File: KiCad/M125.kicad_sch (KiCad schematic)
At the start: 20 parts, among them J1 Conn_01x04, J2 Conn_01x04, J3 Shelly, Q1 PMF250XNEX, U1 ESP32-PICO-MINI-02, U2 LMR16006+FB

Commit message: New PCB
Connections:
- net B: now also U1.35 (IO21); no longer U1.27 (IO7)
- net DATA: now also U1.12 (IO32); no longer U1.21 (IO15)
- net NFCRX: now also U1.28 (IO8); no longer U1.20 (IO13)
- net NFCTX: now also U1.27 (IO7); no longer U1.18 (IO14)
- net SEND: now also U1.13 (IO33); no longer U1.28 (IO8)
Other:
- title: Generic ESP32-PICO-MINI module -> M-125 control
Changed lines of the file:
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@@
   (paper "A4")
   (title_block
-    (title "Generic ESP32-PICO-MINI module")
+    (title "M-125 control")
     (date "${DATE}")
     (rev "1")
@@
   (no_connect (at 50.8 66.04))
   (no_connect (at 50.8 71.12))
-  (no_connect (at 50.8 78.74))
-  (no_connect (at 81.28 68.58))
-  (no_connect (at 81.28 81.28))
-  (no_connect (at 81.28 83.82))
+  (no_connect (at 50.8 81.28))
+  (no_connect (at 91.44 76.2))
+  (no_connect (at 91.44 78.74))
+  (no_connect (at 91.44 81.28))
   (wire (pts (xy 220.98 38.1) (xy 231.775 38.1))
     (stroke (width 0) (type default) (color 0 0 0 0))
@@
     )
   )
-  (global_label "NFCRX" (shape input) (at 50.8 81.28 180) (fields_autoplaced)
-    (effects (font (size 1.27 1.27)) (justify right))
-    (property "Intersheet References" "${INTERSHEET_REFS}" (id 0) (at 42.3072 81.2006 0)
+  (global_label "NFCRX" (shape input) (at 50.8 76.2 180) (fields_autoplaced)
+    (effects (font (size 1.27 1.27)) (justify right))
+    (property "Intersheet References" "${INTERSHEET_REFS}" (id 0) (at 42.3072 76.1206 0)
       (effects (font (size 1.27 1.27)) (justify right) hide)
     )
@@
     )
   )
-  (global_label "SEND" (shape output) (at 50.8 76.2 180) (fields_autoplaced)
-    (effects (font (size 1.27 1.27)) (justify right))
-    (property "Intersheet References" "${INTERSHEET_REFS}" (id 0) (at 43.5168 76.1206 0)
-      (effects (font (size 1.27 1.27)) (justify right) hide)
+  (global_label "SEND" (shape output) (at 81.28 83.82 0) (fields_autoplaced)
+    (effects (font (size 1.27 1.27)) (justify left))
+    (property "Intersheet References" "${INTERSHEET_REFS}" (id 0) (at 88.5632 83.8994 0)
+      (effects (font (size 1.27 1.27)) (justify left) hide)
     )
   )
@@
     )
   )
-  (global_label "DATA" (shape input) (at 50.8 86.36 180) (fields_autoplaced)
-    (effects (font (size 1.27 1.27)) (justify right))
-    (property "Intersheet References" "${INTERSHEET_REFS}" (id 0) (at 44.061 86.2806 0)
-      (effects (font (size 1.27 1.27)) (justify right) hide)
+  (global_label "DATA" (shape input) (at 81.28 81.28 0) (fields_autoplaced)
+    (effects (font (size 1.27 1.27)) (justify left))
+    (property "Intersheet References" "${INTERSHEET_REFS}" (id 0) (at 88.019 81.3594 0)
+      (effects (font (size 1.27 1.27)) (justify left) hide)
     )
   )
@@
     )
   )
-  (global_label "NFCTX" (shape input) (at 50.8 83.82 180) (fields_autoplaced)
-    (effects (font (size 1.27 1.27)) (justify right))
-    (property "Intersheet References" "${INTERSHEET_REFS}" (id 0) (at 42.6096 83.7406 0)
+  (global_label "NFCTX" (shape input) (at 50.8 73.66 180) (fields_autoplaced)
+    (effects (font (size 1.27 1.27)) (justify right))
+    (property "Intersheet References" "${INTERSHEET_REFS}" (id 0) (at 42.6096 73.5806 0)
       (effects (font (size 1.27 1.27)) (justify right) hide)
     )
@@
     )
   )
-  (global_label "B" (shape input) (at 50.8 73.66 180) (fields_autoplaced)
-    (effects (font (size 1.27 1.27)) (justify right))
-    (property "Intersheet References" "${INTERSHEET_REFS}" (id 0) (at -52.07 -31.75 0)
-      (effects (font (size 1.27 1.27)) hide)
-    )
+  (global_label "B" (shape input) (at 81.28 68.58 0) (fields_autoplaced)
+    (effects (font (size 1.27 1.27)) (justify left))
+    (property "Intersheet References" "${INTERSHEET_REFS}" (id 0) (at 184.15 173.99 0)
+      (effects (font (size 1.27 1.27)) hide)
+    )

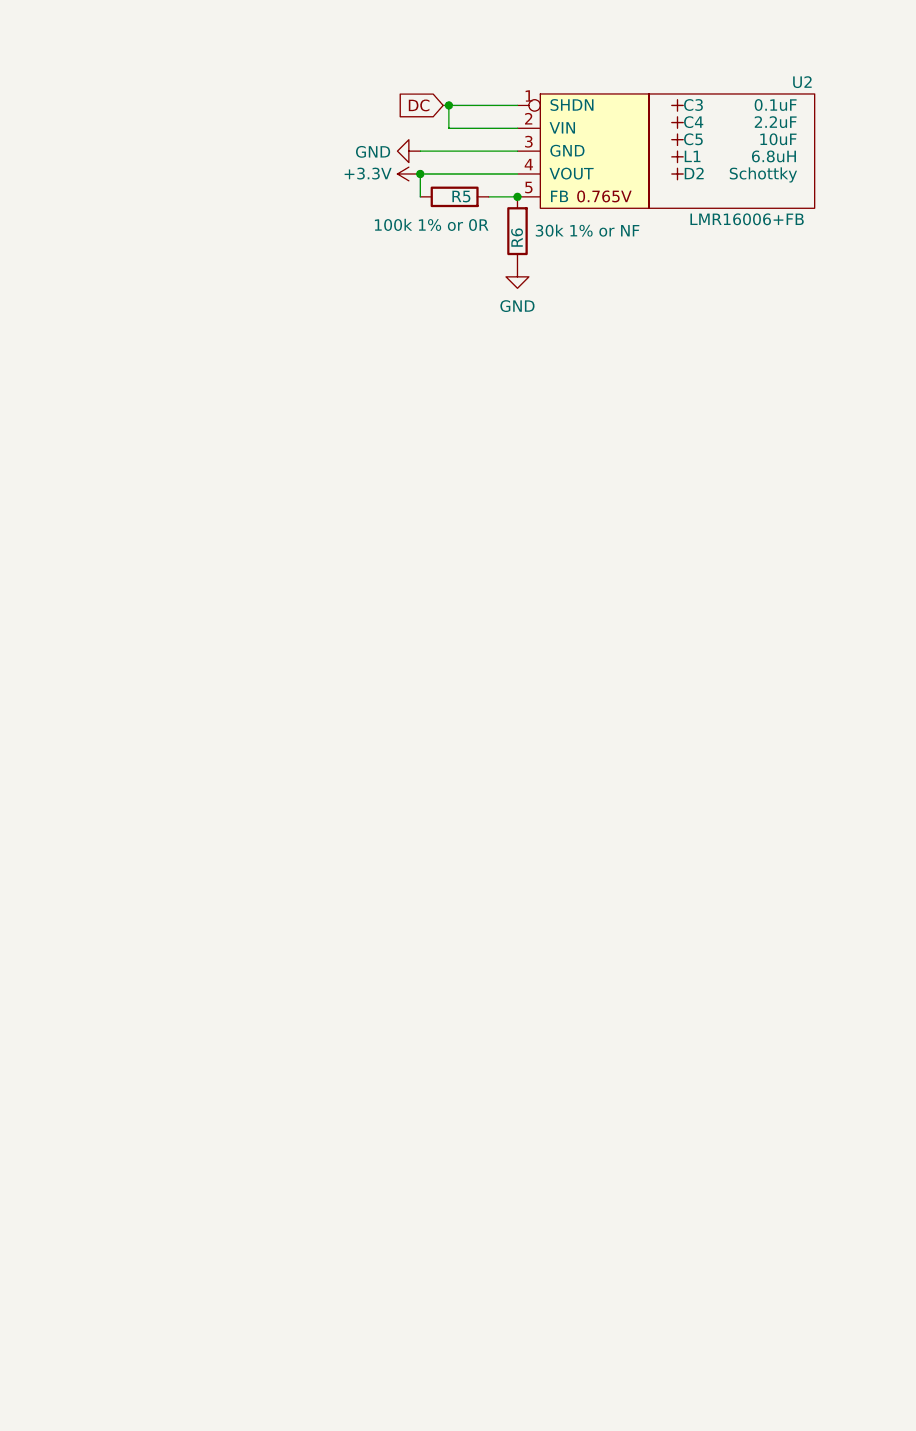
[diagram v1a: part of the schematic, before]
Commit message: Tidy PCB for placement of regulator parts
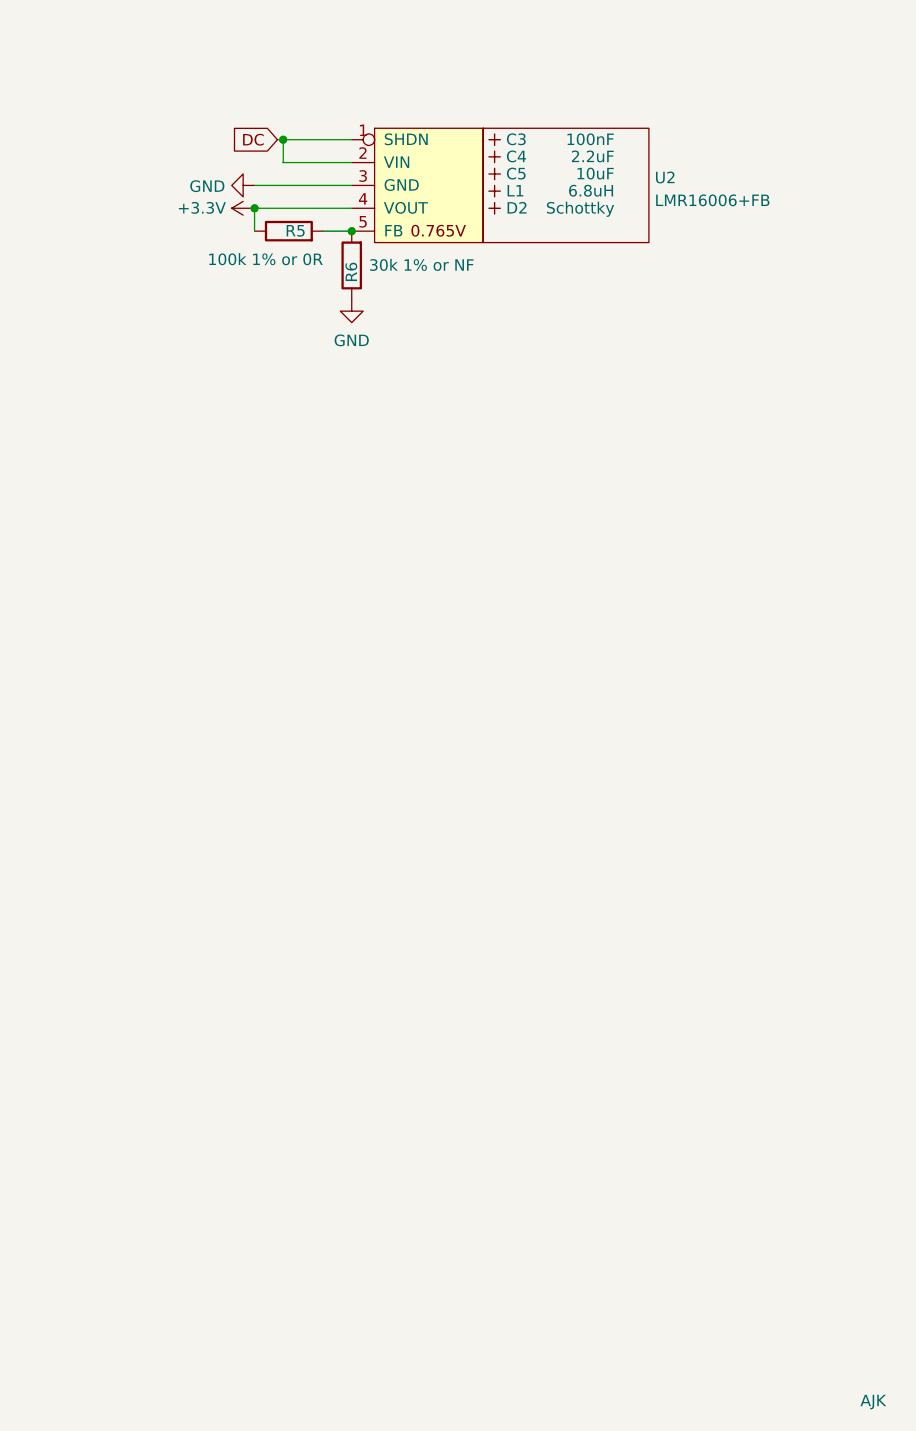
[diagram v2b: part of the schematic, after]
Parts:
- added Logo1: AJK, RevK:AJK, symbol RevK:AJK
- C3: value 0.1uF -> 100nF; footprint RevK:Hidden -> RevK:C_0603_
- C4, C5: footprint RevK:Hidden -> RevK:C_0805_
- D2: footprint RevK:Hidden -> RevK:D_1206_
- L1: footprint RevK:Hidden -> RevK:L_4x4_
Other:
- moved on the sheet: R5, R6
